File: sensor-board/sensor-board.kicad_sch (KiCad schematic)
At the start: 12 parts, among them J1 SM04B-SRSS-TB, U1 HDC2010YPAR, U2 HP203B

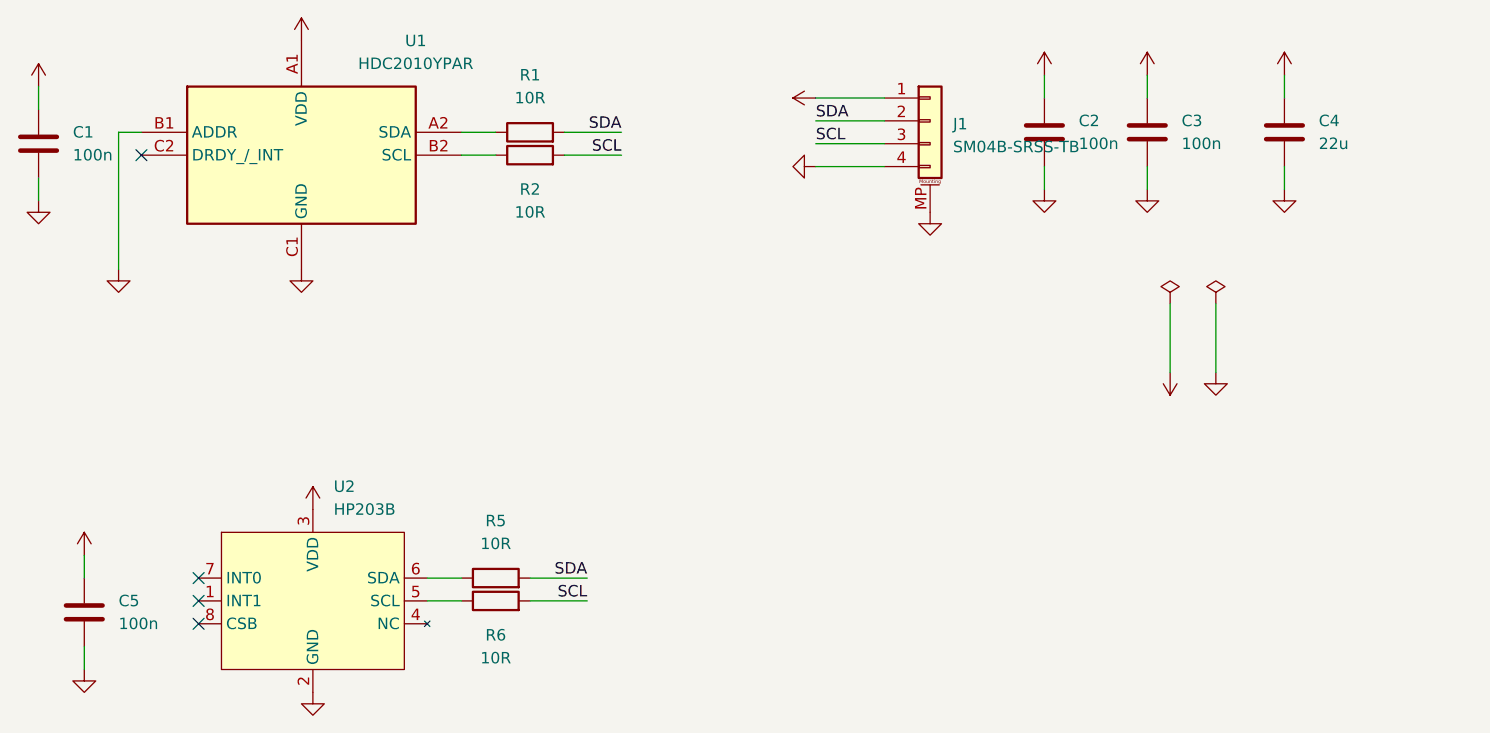
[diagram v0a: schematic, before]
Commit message: sensor-board: Create basic PCB layout
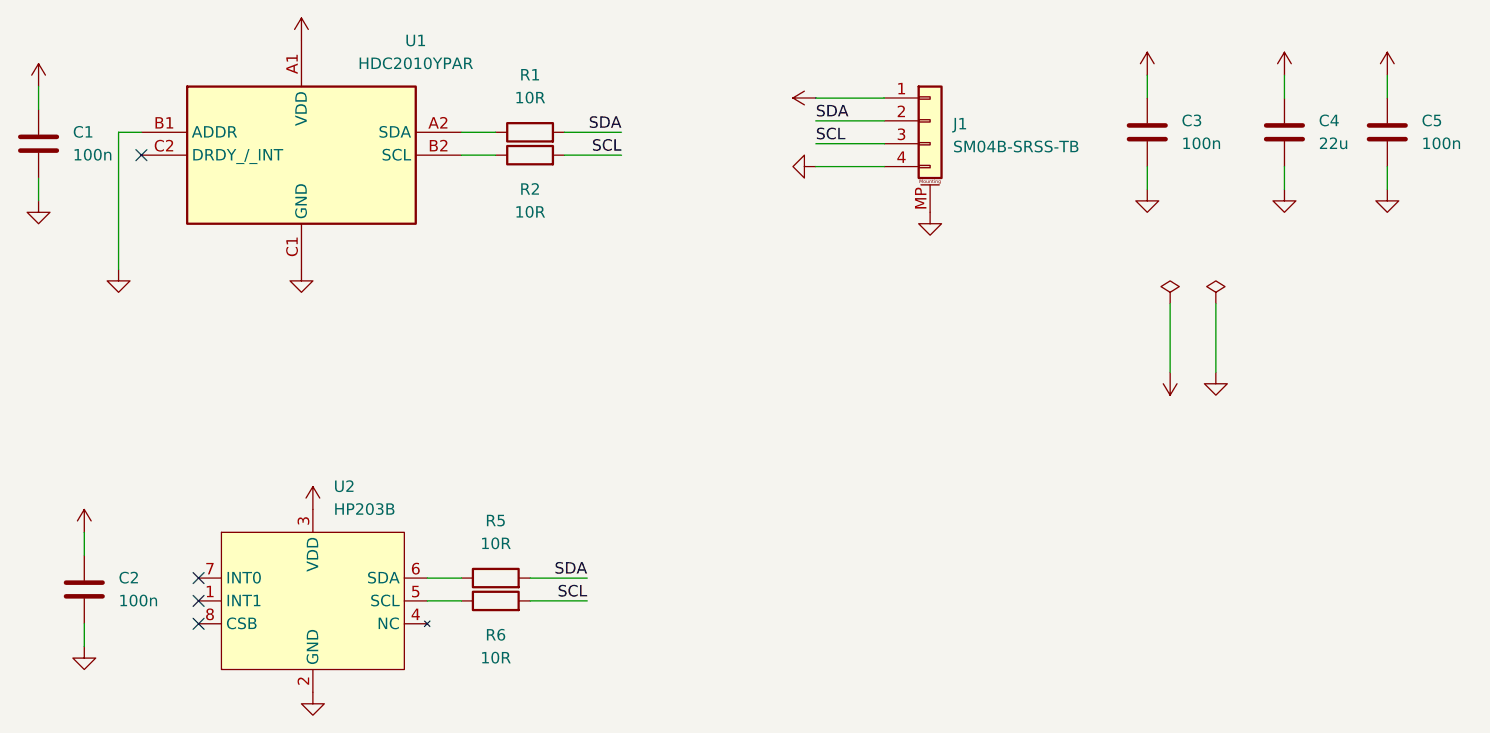
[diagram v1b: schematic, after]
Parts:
- C1, C2, C3, C5: footprint njordr:C_0603_1608Metric_Pad1.08x0.95mm_HandSolder -> njordr:C-0603-HandSolder
- C4: footprint njordr:C_0603_1608Metric_Pad1.08x0.95mm_HandSolder -> njordr:C-0805-HandSolder
- R1, R2, R5, R6: footprint njordr:R_0603_1608Metric_Pad0.98x0.95mm_HandSolder -> njordr:R-0603-HandSolder
- U1: footprint njordr:DSBGA-6-1.49x1.49 -> njordr:DSBGA-6-1.5x1.5
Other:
- moved on the sheet: C2, C5
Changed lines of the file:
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@@
 	(wire
 		(pts
-			(xy 64.77 143.51) (xy 64.77 146.05)
+			(xy 209.55 90.17) (xy 209.55 92.71)
 		)
 		(stroke
@@
 	(wire
 		(pts
-			(xy 171.45 80.01) (xy 171.45 82.55)
+			(xy 64.77 130.81) (xy 64.77 133.35)
 		)
 		(stroke
@@
 	(wire
 		(pts
-			(xy 171.45 90.17) (xy 171.45 92.71)
+			(xy 64.77 140.97) (xy 64.77 143.51)
 		)
 		(stroke
@@
 	(wire
 		(pts
-			(xy 64.77 133.35) (xy 64.77 135.89)
+			(xy 209.55 80.01) (xy 209.55 82.55)
 		)
 		(stroke
@@
 			)
 		)
-		(property "Footprint" "njordr:C_0603_1608Metric_Pad1.08x0.95mm_HandSolder"
+		(property "Footprint" "njordr:C-0603-HandSolder"
 			(at 60.6552 91.44 0)
 			(effects
@@
 	(symbol
 		(lib_id "power:VCC")
-		(at 64.77 133.35 0)
+		(at 209.55 80.01 0)
 		(unit 1)
 		(exclude_from_sim no)
@@
 		(fields_autoplaced yes)
 		(property "Reference" "#PWR019"
-			(at 64.77 137.16 0)
+			(at 209.55 83.82 0)
 			(effects
 				(font
@@
 		)
 		(property "Value" "VCC"
-			(at 64.77 128.27 0)
+			(at 209.55 74.93 0)
 			(effects
 				(font
@@
 		)
 		(property "Footprint" ""
-			(at 64.77 133.35 0)
+			(at 209.55 80.01 0)
 			(effects
 				(font
@@
 		)
 		(property "Datasheet" ""
-			(at 64.77 133.35 0)
+			(at 209.55 80.01 0)
 			(effects
 				(font
@@
 		)
 		(property "Description" "Power symbol creates a global label with name \"VCC\""
-			(at 64.77 133.35 0)
+			(at 209.55 80.01 0)
 			(effects
 				(font
@@
 			)
 		)
-		(property "Footprint" "njordr:DSBGA-6-1.49x1.49"
+		(property "Footprint" "njordr:DSBGA-6-1.5x1.5"
 			(at 102.87 178.74 0)
 			(effects
@@
 			)
 		)
-		(property "Footprint" "njordr:C_0603_1608Metric_Pad1.08x0.95mm_HandSolder"
+		(property "Footprint" "njordr:C-0603-HandSolder"
 			(at 183.8452 90.17 0)
 			(effects
@@
 	(symbol
 		(lib_id "power:VCC")
-		(at 171.45 80.01 0)
+		(at 64.77 130.81 0)
 		(unit 1)
 		(exclude_from_sim no)
@@
 		(fields_autoplaced yes)
 		(property "Reference" "#PWR011"
-			(at 171.45 83.82 0)
+			(at 64.77 134.62 0)
 			(effects
 				(font
@@
 		)
 		(property "Value" "VCC"
-			(at 171.45 74.93 0)
+			(at 64.77 125.73 0)
 			(effects
 				(font
@@
 		)
 		(property "Footprint" ""
-			(at 171.45 80.01 0)
+			(at 64.77 130.81 0)
 			(effects
 				(font
@@
 		)
 		(property "Datasheet" ""
-			(at 171.45 80.01 0)
+			(at 64.77 130.81 0)
 			(effects
 				(font
@@
 		)
 		(property "Description" "Power symbol creates a global label with name \"VCC\""
-			(at 171.45 80.01 0)
+			(at 64.77 130.81 0)
 			(effects
 				(font
@@
 			)
 		)
-		(property "Footprint" "njordr:R_0603_1608Metric_Pad0.98x0.95mm_HandSolder"
+		(property "Footprint" "njordr:R-0603-HandSolder"
 			(at 110.49 140.208 90)
 			(effects
@@
 			)
 		)
-		(property "Footprint" "njordr:C_0603_1608Metric_Pad1.08x0.95mm_HandSolder"
+		(property "Footprint" "njordr:C-0805-HandSolder"
 			(at 199.0852 90.17 0)
 			(effects
@@
 			)
 		)
-		(property "Footprint" "njordr:R_0603_1608Metric_Pad0.98x0.95mm_HandSolder"
+		(property "Footprint" "njordr:R-0603-HandSolder"
 			(at 114.3 88.138 90)
 			(effects
@@
 	(symbol
 		(lib_id "Device:C")
-		(at 171.45 86.36 0)
+		(at 64.77 137.16 0)
 		(unit 1)
 		(exclude_from_sim no)
@@
 		(fields_autoplaced yes)
 		(property "Reference" "C2"
-			(at 175.26 85.0899 0)
+			(at 68.58 135.8899 0)
 			(effects
 				(font
@@
 		)
 		(property "Value" "100n"
-			(at 175.26 87.6299 0)
+			(at 68.58 138.4299 0)
 			(effects
 				(font
@@
 			)
 		)
-		(property "Footprint" "njordr:C_0603_1608Metric_Pad1.08x0.95mm_HandSolder"
-			(at 172.4152 90.17 0)
+		(property "Footprint" "njordr:C-0603-HandSolder"
+			(at 65.7352 140.97 0)
 			(effects
 				(font
@@
 		)
 		(property "Datasheet" "~"
-			(at 171.45 86.36 0)
+			(at 64.77 137.16 0)
 			(effects
 				(font
@@
 		)
 		(property "Description" "Unpolarized capacitor"
-			(at 171.45 86.36 0)
+			(at 64.77 137.16 0)
 			(effects
 				(font
@@
 		)
 		(property "LCSC" "C14663"
-			(at 171.45 86.36 0)
+			(at 64.77 137.16 0)
 			(effects
 				(font
@@
 	(symbol
 		(lib_id "power:GND")
-		(at 171.45 92.71 0)
+		(at 64.77 143.51 0)
 		(unit 1)
 		(exclude_from_sim no)
@@
 		(fields_autoplaced yes)
 		(property "Reference" "#PWR012"
-			(at 171.45 99.06 0)
+			(at 64.77 149.86 0)
 			(effects
 				(font
@@
 		)
 		(property "Value" "GND"
-			(at 171.45 97.79 0)
+			(at 64.77 148.59 0)
 			(effects
 				(font
@@
 		)
 		(property "Footprint" ""
-			(at 171.45 92.71 0)
+			(at 64.77 143.51 0)
 			(effects
 				(font
@@
 		)
 		(property "Datasheet" ""
-			(at 171.45 92.71 0)
+			(at 64.77 143.51 0)
 			(effects
 				(font
@@
 		)
 		(property "Description" "Power symbol creates a global label with name \"GND\" , ground"
-			(at 171.45 92.71 0)
+			(at 64.77 143.51 0)
 			(effects
 				(font
@@
 			)
 		)
-		(property "Footprint" "njordr:R_0603_1608Metric_Pad0.98x0.95mm_HandSolder"
+		(property "Footprint" "njordr:R-0603-HandSolder"
 			(at 114.3 90.678 90)
 			(effects
@@
 	(symbol
 		(lib_id "power:GND")
-		(at 64.77 146.05 0)
+		(at 209.55 92.71 0)
 		(unit 1)
 		(exclude_from_sim no)
@@
 		(fields_autoplaced yes)
 		(property "Reference" "#PWR020"
-			(at 64.77 152.4 0)
+			(at 209.55 99.06 0)
 			(effects
 				(font
@@
 		)
 		(property "Value" "GND"
-			(at 64.77 151.13 0)
+			(at 209.55 97.79 0)
 			(effects
 				(font
@@
 		)
 		(property "Footprint" ""
-			(at 64.77 146.05 0)
+			(at 209.55 92.71 0)
 			(effects
 				(font
@@
 		)
 		(property "Datasheet" ""
-			(at 64.77 146.05 0)
+			(at 209.55 92.71 0)
 			(effects
 				(font
@@
 		)
 		(property "Description" "Power symbol creates a global label with name \"GND\" , ground"
-			(at 64.77 146.05 0)
+			(at 209.55 92.71 0)
 			(effects
 				(font
@@
 	(symbol
 		(lib_id "Device:C")
-		(at 64.77 139.7 0)
+		(at 209.55 86.36 0)
 		(unit 1)
 		(exclude_from_sim no)
@@
 		(fields_autoplaced yes)
 		(property "Reference" "C5"
-			(at 68.58 138.4299 0)
+			(at 213.36 85.0899 0)
 			(effects
 				(font
@@
 		)
 		(property "Value" "100n"
-			(at 68.58 140.9699 0)
+			(at 213.36 87.6299 0)
 			(effects
 				(font
@@
 			)
 		)
-		(property "Footprint" "njordr:C_0603_1608Metric_Pad1.08x0.95mm_HandSolder"
-			(at 65.7352 143.51 0)
+		(property "Footprint" "njordr:C-0603-HandSolder"
+			(at 210.5152 90.17 0)
 			(effects
 				(font
@@
 		)
 		(property "Datasheet" "~"
-			(at 64.77 139.7 0)
+			(at 209.55 86.36 0)
 			(effects
 				(font
@@
 		)
 		(property "Description" "Unpolarized capacitor"
-			(at 64.77 139.7 0)
+			(at 209.55 86.36 0)
 			(effects
 				(font
@@
 		)
 		(property "LCSC" "C14663"
-			(at 64.77 139.7 0)
+			(at 209.55 86.36 0)
 			(effects
 				(font
@@
 			)
 		)
-		(property "Footprint" "njordr:R_0603_1608Metric_Pad0.98x0.95mm_HandSolder"
+		(property "Footprint" "njordr:R-0603-HandSolder"
 			(at 110.49 137.668 90)
 			(effects

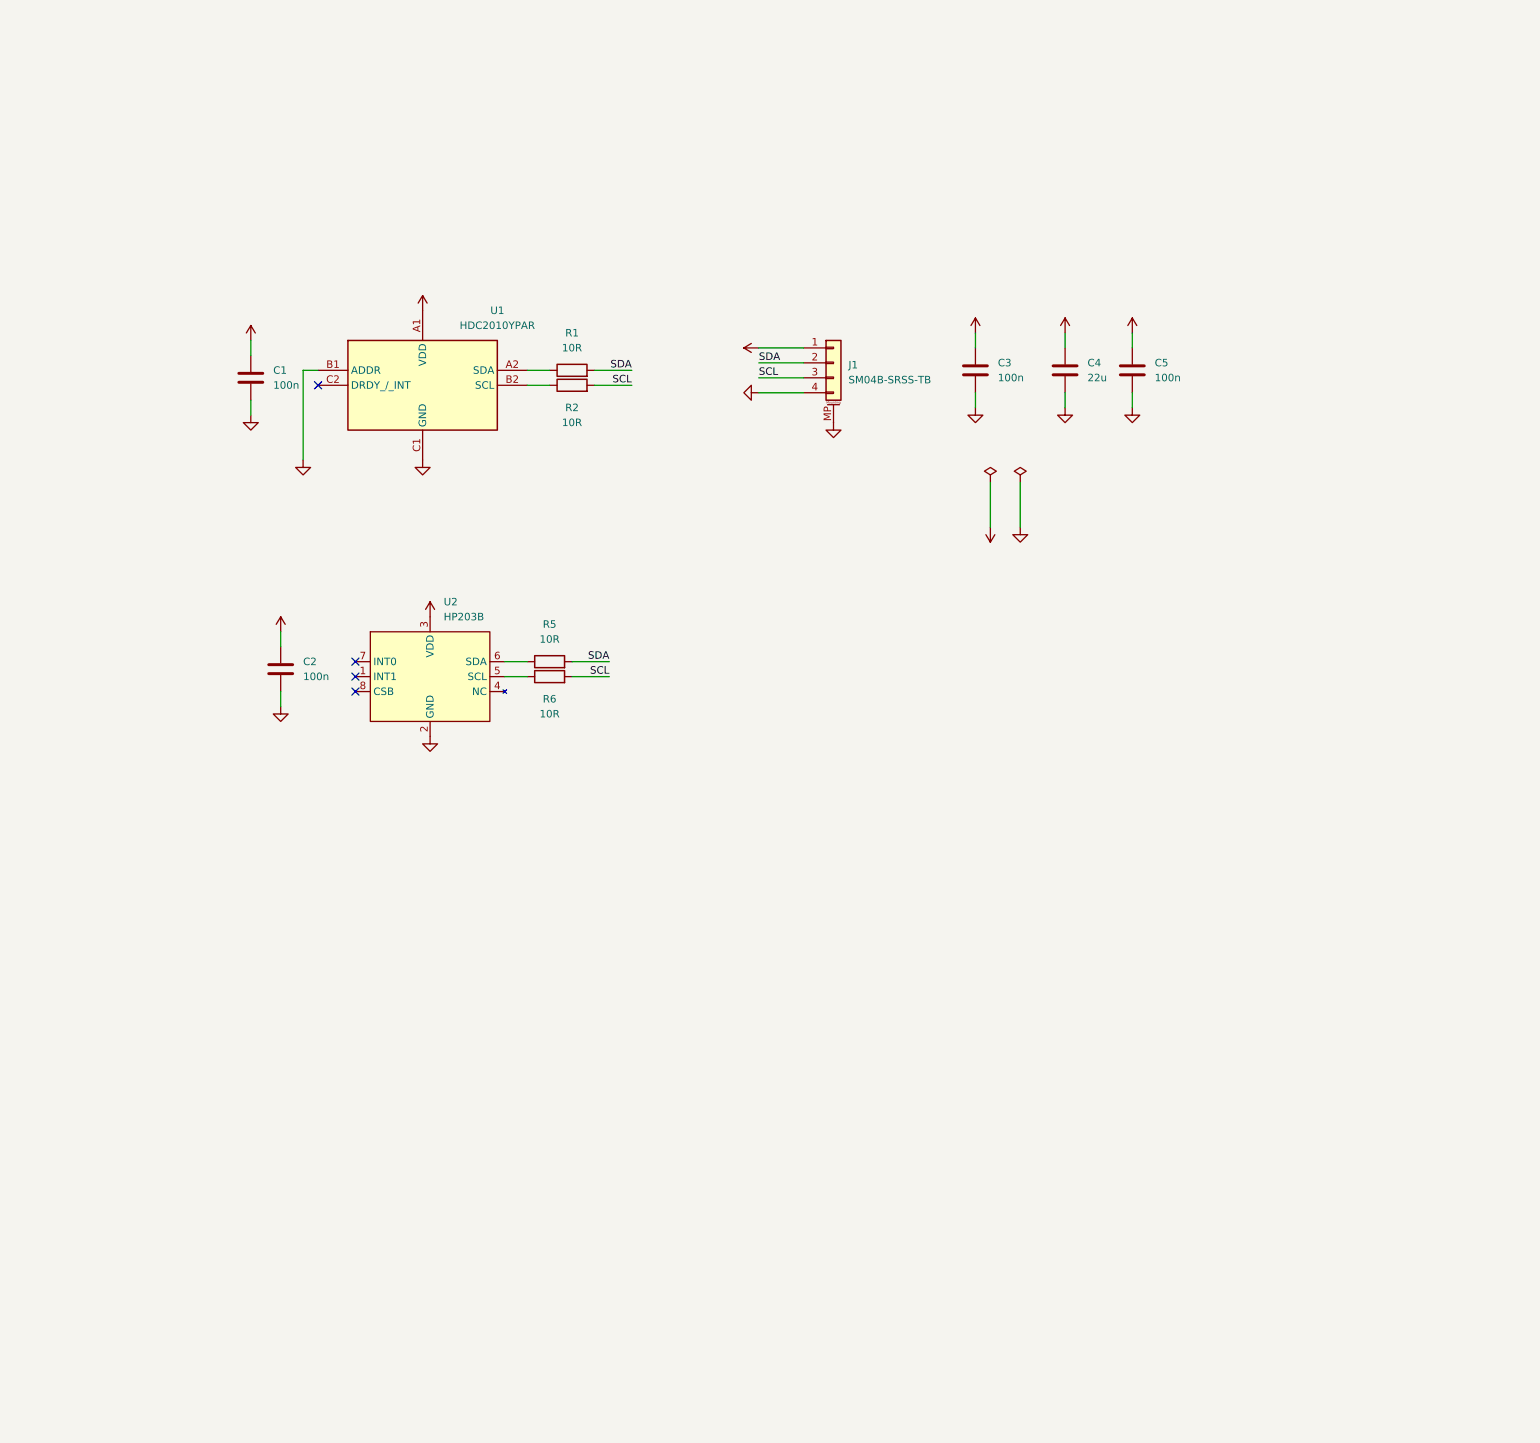
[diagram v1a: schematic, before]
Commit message: sensor-board: Finalize the first iteration
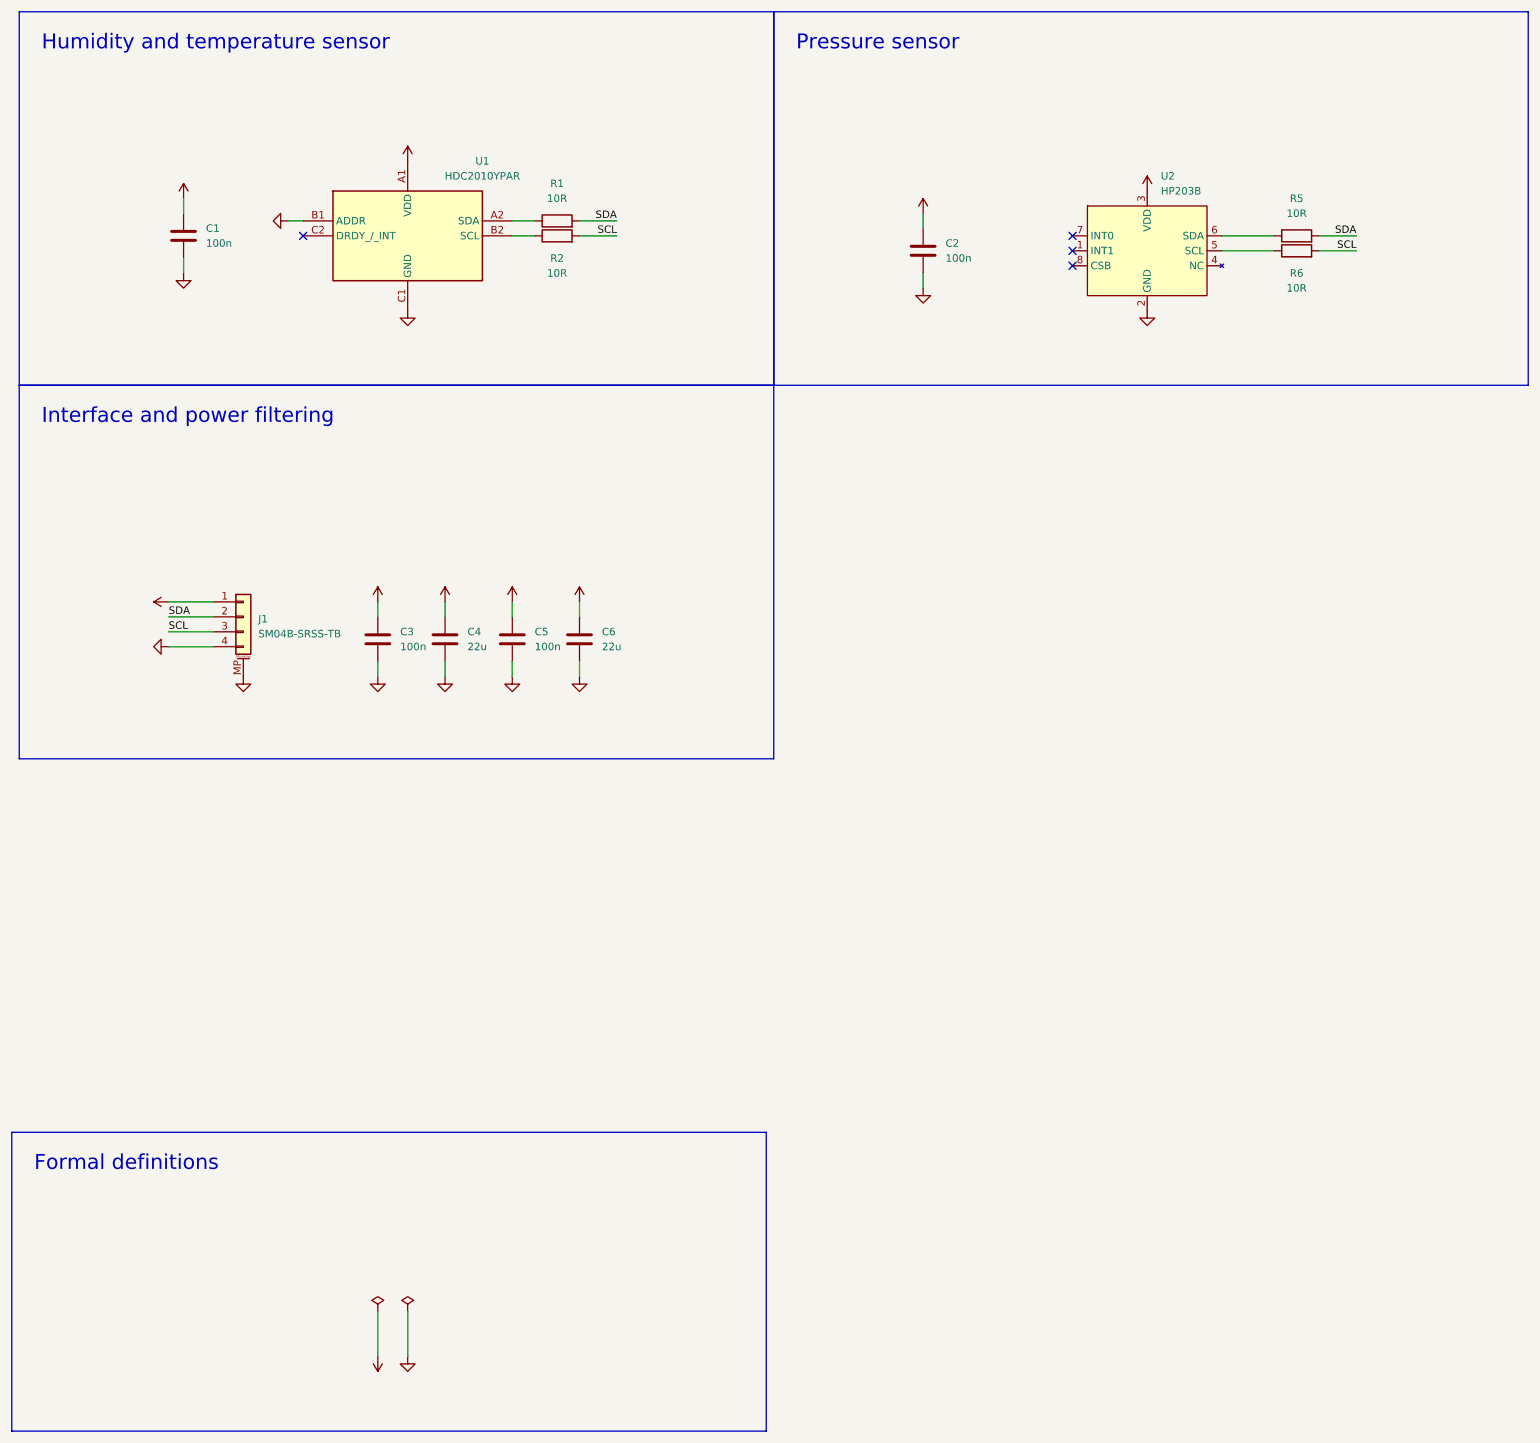
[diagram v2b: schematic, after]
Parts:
- added C6: 22u, njordr:C-0805-HandSolder, symbol Device:C
- U1: symbol HDC2010YPAR:HDC2010YPAR -> njordr:HDC2010YPAR; Height 0.7 -> 0
- U2: LCSC (none) -> C138665
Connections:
- net GND: now also C6.2
- net VCC: now also C6.1
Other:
- note added: "Formal definitions"
- note added: "Humidity and temperature sensor"
- note added: "Interface and power filtering"
- note added: "Pressure sensor"
- title: (none) -> SENSOR BOARD
- moved on the sheet: C1, C2, C3, C4, C5, J1, R1, R2, R5, R6, U1, U2
